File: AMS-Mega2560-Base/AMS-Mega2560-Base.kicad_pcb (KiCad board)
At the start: 4 copper layers, 168.7 x 106.7 mm, 224 parts, among them IC1 CD74HC4050ME4, IC10 LM2597MX-ADJ_NOPB, IC11 LM2597M-3.3_NOPB, IC12 OPA2340PA, IC13 MAX764CPA+, IC14 LM2917N-8_NOPB, IC15 MAX31865AAP+, IC16 DS3231SN#, IC17 MAX232CPE+, IC18 MAX31865AAP+, IC19 MAX6326UR31+T, IC2 CD74HC4050ME4, IC3 MAX31865AAP+, IC4 MAX31865AAP+, IC5 MAX31865AAP+, IC6 OPA2340PA, IC7 LTV-846S, IC8 MAX31865AAP+, IC9 LM2670SX-5.0_NOPB, J1 RTD1, J10 Conn_01x03, J11 Conn_01x02, J12 Conn_01x02, J13 Conn_01x03, J14 Conn_01x02, J15 Conn_01x02, J16 Conn_01x03, J17 Conn_01x02, J18 Conn_01x02, J19 Conn_01x03, J2 RTD2, J20 Conn_01x02, J21 Screw_Terminal_01x03, J22 Conn_01x07, J23 Conn_01x02, J24 Conn_01x02, J25 Conn_01x02, J26 Conn_01x03, J27 Conn_01x02, J28 Conn_01x02, J29 Conn_01x03, J3 Conn_01x08, J30 Conn_01x02, J31 Conn_01x02, J32 Conn_01x02, J4 Sense1, J5 Sense2, J6 AdafruitUltimateGPS, J7 Conn_02x03_Odd_Even, J8 Conn_01x03, J9 Conn_01x02, P1 Power, P10 CONN_01X01, P11 CONN_01X01, P12 CONN_01X01, P13 CONN_01X01, P2 Analog, P3 Analog, P4 Digital, P5 PWM, P6 PWM, P7 Communication, P8 CONN_01X01, P9 CONN_01X01, Q1 2N7000, Q10 IRF9Z34NPBF, Q11 2N7000, Q12 2N7000, Q13 IRF9Z34NPBF, Q14 IRF9Z34NPBF, Q15 2N7000, Q16 2N7000, Q17 IRF9Z34NPBF, Q18 IRF9Z34NPBF, Q19 2N7000, Q2 2N7000, Q20 IRF9Z34NPBF, Q21 IRF9Z34NPBF, Q22 BD140, Q23 2N7000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

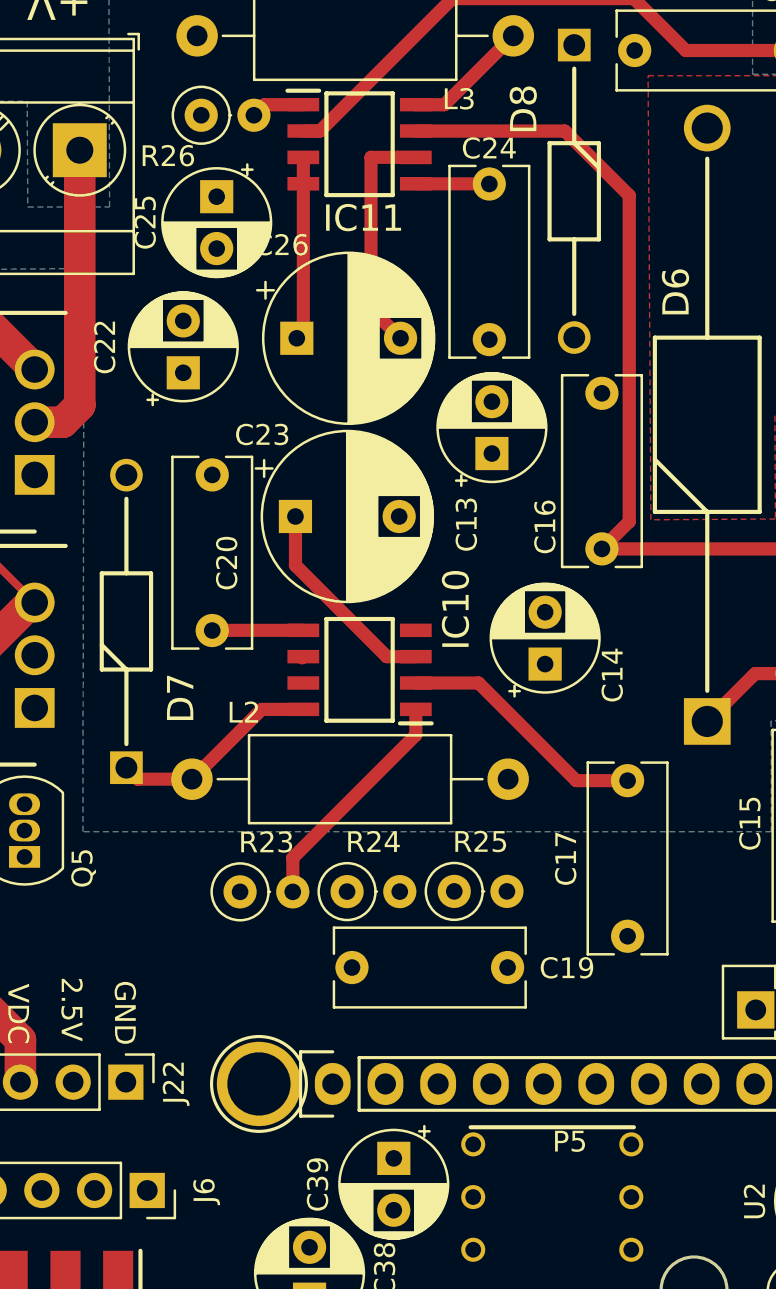
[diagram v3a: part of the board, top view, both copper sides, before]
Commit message: Schematic ERC is done and DRC for current layout is done. Need to verify a new part of the circuit before routing the rest of the board.
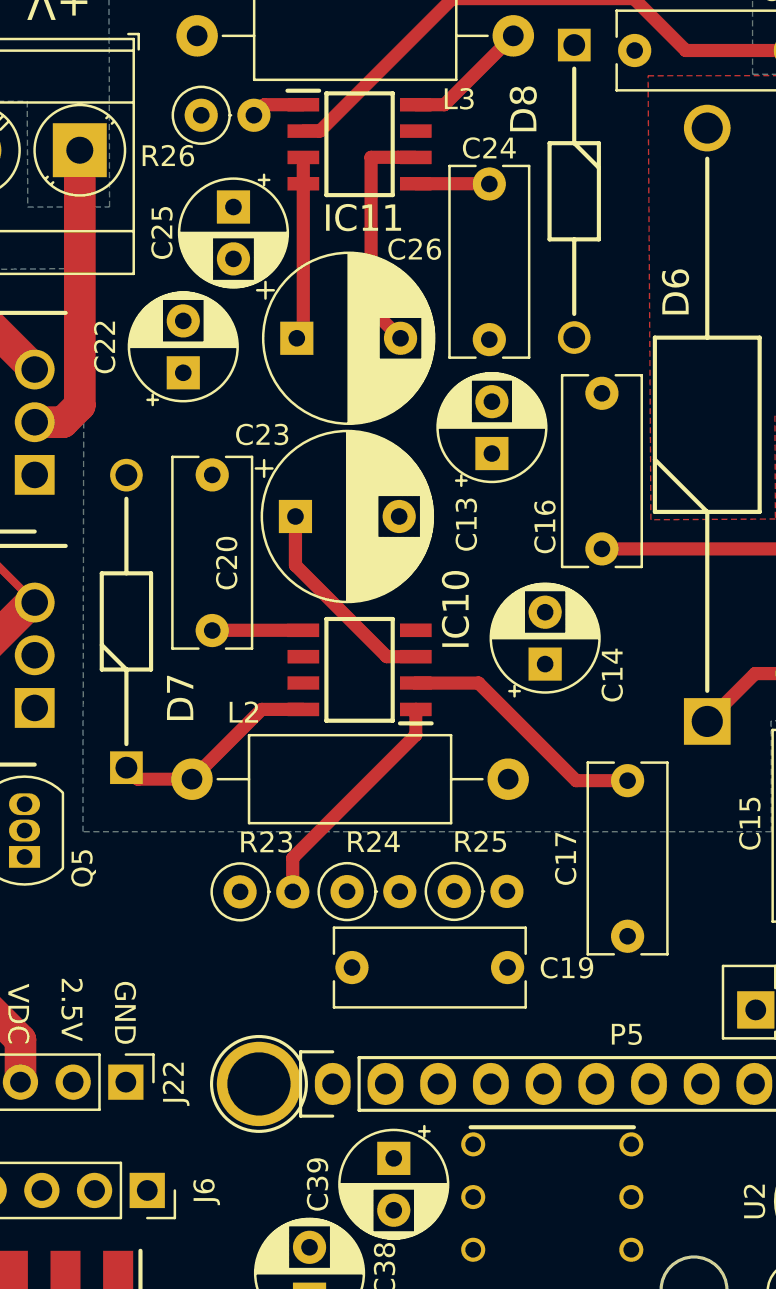
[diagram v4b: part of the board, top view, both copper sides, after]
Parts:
- moved C25 0.95 mm to (98.1, 58.5)
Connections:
- net /Ambient renamed 3VAmbientCS
- net /Carb renamed 3VCarbCS
- net /FrontT renamed 3VFrontCS
- net /LsideT renamed 3VLsideCS
- net /RsideT renamed 3VRsideCS
- net /WaterT renamed 3VWaterCS
- net IN1 renamed IN1TTL
- net IN2 renamed IN2TTL
- net IN3 renamed IN3TTL
- C18 pad 1: +5VP -> +5V
- C36 pad 1: +5VP -> +5V
- C40 pad 2: +5VP -> +5V
- IC1 pad 2: SCLK -> 3VSCLK
- IC1 pad 4: MOSI -> 3VMOSI
- IC1 pad 7: MISO -> 3VMISO
- IC12 pad 8: +5VP -> +5V
- IC15 pad 14: MOSI -> 3VMOSI
- IC15 pad 15: SCLK -> 3VSCLK
- IC15 pad 17: MISO -> 3VMISO
- IC16 pad 2: +5VP -> +5V
- IC17 pad 16: +5VP -> +5V
- IC18 pad 14: MOSI -> 3VMOSI
- IC18 pad 15: SCLK -> 3VSCLK
- IC18 pad 17: MISO -> 3VMISO
- IC3 pad 14: MOSI -> 3VMOSI
- IC3 pad 15: SCLK -> 3VSCLK
- IC3 pad 17: MISO -> 3VMISO
- IC4 pad 14: MOSI -> 3VMOSI
- IC4 pad 15: SCLK -> 3VSCLK
- IC4 pad 17: MISO -> 3VMISO
- IC5 pad 14: MOSI -> 3VMOSI
- IC5 pad 15: SCLK -> 3VSCLK
- IC5 pad 17: MISO -> 3VMISO
- IC8 pad 14: MOSI -> 3VMOSI
- IC8 pad 15: SCLK -> 3VSCLK
- IC8 pad 17: MISO -> 3VMISO
- IC9 pad 6: +5VP -> +5V
- J22 pad 4: +5VP -> +5V
- J3 pad 1: +5VP -> +5V
- J6 pad 1: /3.3 -> unconnected-(J6-Pad1)
- J6 pad 2: /EN -> unconnected-(J6-Pad2)
- J6 pad 4: /FIX -> unconnected-(J6-Pad4)
- J6 pad 8: +5VP -> +5V
- J6 pad 9: /PPS -> unconnected-(J6-Pad9)
- J7 pad 1: +5VP -> +5V
- L1 pad 2: +5VP -> +5V
- P1 pad 2: /IOREF -> unconnected-(P1-Pad2)
- P1 pad 3: /Reset -> unconnected-(P1-Pad3)
- P1 pad 4: +3V3 -> unconnected-(P1-Pad4)
- P1 pad 5: +5V -> unconnected-(P1-Pad5)
- P3 pad 7: /A14 -> unconnected-(P3-Pad7)
- P3 pad 8: /A15 -> unconnected-(P3-Pad8)
- P4 pad 16: /41 -> unconnected-(P4-Pad16)
- P4 pad 18: /39 -> unconnected-(P4-Pad18)
- P4 pad 20: /37 -> unconnected-(P4-Pad20)
- P4 pad 22: /35 -> unconnected-(P4-Pad22)
- P4 pad 23: /32 -> unconnected-(P4-Pad23)
- P4 pad 24: /33 -> unconnected-(P4-Pad24)
- P4 pad 25: /30 -> unconnected-(P4-Pad25)
- P4 pad 26: /31 -> unconnected-(P4-Pad26)
- P4 pad 27: /28 -> unconnected-(P4-Pad27)
- P4 pad 28: /29 -> unconnected-(P4-Pad28)
- P4 pad 29: /26 -> unconnected-(P4-Pad29)
- P4 pad 30: /27 -> unconnected-(P4-Pad30)
- P4 pad 31: /24 -> unconnected-(P4-Pad31)
- P4 pad 32: /25 -> unconnected-(P4-Pad32)
- P4 pad 33: /22 -> unconnected-(P4-Pad33)
- P4 pad 34: /23 -> unconnected-(P4-Pad34)
- P4 pad 35: +5V -> unconnected-(P4-Pad35)
- P4 pad 36: +5V -> unconnected-(P4-Pad36)
- P4 pad 4: /53(SS) -> unconnected-(P4-Pad4)
- P5 pad 3: /AREF -> unconnected-(P5-Pad3)
- P5 pad 5: /13(**) -> unconnected-(P5-Pad5)
- P5 pad 6: /12(**) -> unconnected-(P5-Pad6)
- P5 pad 7: /11(**) -> unconnected-(P5-Pad7)
- P5 pad 8: /10(**) -> unconnected-(P5-Pad8)
- P5 pad 9: /9(**) -> unconnected-(P5-Pad9)
- P6 pad 7: /1(Tx0) -> unconnected-(P6-Pad7)
- P6 pad 8: /0(Rx0) -> unconnected-(P6-Pad8)
- P7 pad 5: /18(Tx1) -> unconnected-(P7-Pad5)
- P7 pad 6: /19(Rx1) -> unconnected-(P7-Pad6)
- R1 pad 1: +5VP -> +5V
- R11 pad 1: +5VP -> +5V
- R13 pad 1: +5VP -> +5V
- R14 pad 1: +5VP -> +5V
- R15 pad 1: +5VP -> +5V
- R16 pad 1: +5VP -> +5V
- R17 pad 1: +5VP -> +5V
- R18 pad 1: +5VP -> +5V
- R19 pad 1: +5VP -> +5V
- R31 pad 1: +5VP -> +5V
- R37 pad 1: +5VP -> +5V
- R38 pad 1: +5VP -> +5V
- RV4 pad 1: AUXVoltage1 -> Sense1-11
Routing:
- net +VSW: track 92.2 -> 61.4 mm
- net +5VP: track 28.1 -> 0.00 mm
- net +5V: track 0.00 -> 28.1 mm

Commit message: pushing this change to the repo need to vet some schematics
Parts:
- removed R64: 4.7K, Resistor_THT:R_Axial_DIN0207_L6.3mm_D2.5mm_P2.54mm_Vertical
- Q22: value BD140 -> IRF9610PBF-BE3; footprint Package_TO_SOT_THT:TO-126-3_Vertical -> SamacSys_Parts:TO254P465X1024X2050-3P
- moved Q24 122.8 mm to (156.5, 115.6)
- moved D10 121.6 mm to (149.9, 122.0)
- moved Q22 52.7 mm to (70.6, 95.9), turned to -90 degrees
- moved J22 3.18 mm to (94.4, 97.9)
- moved U1 2.87 mm to (73.4, 73.0)
- moved Q23 2.69 mm to (70.3, 89.5)
- moved R63 2.69 mm to (76.0, 88.3)
- moved IC7 0.73 mm to (83.8, 115.1)
- moved J21 0.62 mm to (91.3, 55.7)
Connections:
- Q1 pad 2: Sense1-10 -> Sense2-1
- Q22 pad 1: +3.3VP -> Net-(Q22-Pad1)
- Q22 pad 3: Net-(Q22-Pad3) -> +3.3VP
- R5 pad 1: Sense1-10 -> Sense2-1
- R63 pad 1: Net-(Q22-Pad3) -> Net-(Q22-Pad1)
- RV3 pad 1: Sense2-1 -> Sense1-10
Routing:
- net +VDC: track 169.9 -> 139.6 mm
- net Net-(Q6-Pad3): track 18.2 -> 17.0 mm
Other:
- board text added: "ON"

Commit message: adding some fixes for the RPM sensor and trying to fit everything on the board. WIp for FW
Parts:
- removed J32: Conn_01x02, Connector_PinHeader_2.54mm:PinHeader_1x02_P2.54mm_Vertical
- removed RV3: 500k, Potentiometer_THT:Potentiometer_Bourns_3296W_Vertical
- added IC20: OPA4340UA, SamacSys_Parts:SOIC127P600X175-14N, F.Cu at (24.3, 123.3)
- added K1: DIP05-1A72-12L, SamacSys_Parts:DIP051A7212L, F.Cu at (205.3, 82.8)
- added Q25: 2N7000, Package_TO_SOT_THT:TO-92_Inline, F.Cu at (212.5, 83.8)
- added R64: 47K, Resistor_THT:R_Axial_DIN0207_L6.3mm_D2.5mm_P2.54mm_Vertical, F.Cu at (30.6, 120.2)
- added R65: 47K, Resistor_THT:R_Axial_DIN0207_L6.3mm_D2.5mm_P2.54mm_Vertical, F.Cu at (30.6, 124.2)
- added R66: 47K, Resistor_THT:R_Axial_DIN0207_L6.3mm_D2.5mm_P2.54mm_Vertical, F.Cu at (36.7, 120.2)
- added R67: 47K, Resistor_THT:R_Axial_DIN0207_L6.3mm_D2.5mm_P2.54mm_Vertical, F.Cu at (30.6, 128.3)
- added R68: 47K, Resistor_THT:R_Axial_DIN0207_L6.3mm_D2.5mm_P2.54mm_Vertical, F.Cu at (47.0, 120.2)
- added R69: 47K, Resistor_THT:R_Axial_DIN0207_L6.3mm_D2.5mm_P2.54mm_Vertical, F.Cu at (53.1, 120.2)
- added R70: R, Resistor_THT:R_Axial_DIN0207_L6.3mm_D2.5mm_P2.54mm_Vertical, F.Cu at (215.0, 89.7)
- IC6: value OPA2340PA -> OPA4340UA; footprint SamacSys_Parts:DIP794W53P254L959H508Q8N -> SamacSys_Parts:SOIC127P600X175-14N
- moved C29 98.5 mm to (297.2, 65.6)
- moved J23 96.0 mm to (271.7, 92.5)
- moved C27 92.8 mm to (273.5, 77.6)
- moved D9 89.7 mm to (287.3, 59.5)
- moved L4 89.7 mm to (273.2, 55.9)
- moved C30 89.7 mm to (266.8, 65.9)
- moved IC13 89.7 mm to (280.0, 66.4)
- moved J24 66.3 mm to (282.3, 91.1)
- moved C28 56.6 mm to (262.1, 80.3)
- moved J31 42.0 mm to (153.3, 133.6)
- moved R46 8.93 mm to (154.9, 95.2)
- moved RV4 5.09 mm to (115.8, 126.8)
- moved C32 4.95 mm to (213.4, 96.6)
- moved R1 4.13 mm to (218.1, 89.7), turned to 90 degrees
- moved R35 3.41 mm to (215.5, 84.5)
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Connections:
- IC14 pad 5: +VDC -> +VSW
- IC17 pad 13: Sense2-8 -> Sense1-8
- IC17 pad 14: Sense2-11 -> Sense1-11
- IC6 pad 1: ThrottlePositionADC -> OilPressure
- IC6 pad 2: ThrottlePositionADC -> OilPressure
- IC6 pad 3: Net-(IC6-Pad3) -> Sense1-10
- IC6 pad 4: GND -> +5V
- IC6 pad 5: Net-(IC6-Pad5) -> Sense1-7
- IC6 pad 6: SpareBufferedADC -> AFR1
- IC6 pad 7: SpareBufferedADC -> AFR1
- IC6 pad 8: +5V -> AFR2
- J31 pad 1: Net-(IC6-Pad3) -> Net-(RV2-Pad2)
- J31 pad 2: Net-(J31-Pad2) -> /A10
- J4 pad 12: AltCurrent -> Sense1-12
- J4 pad 2: OilPressure -> SCL
- J4 pad 5: FuelPressure1 -> SDA
- J4 pad 6: AFR1 -> Sense1-6
- J4 pad 8: FuelPressure2 -> Sense1-8
- J4 pad 9: AFR2 -> Sense1-9
- J5 pad 2: SCL -> Sense2-2
- J5 pad 5: SDA -> Sense2-5
- Q10 pad 2: Sense1-7 -> Sense2-11
- Q13 pad 2: Sense2-6 -> Sense2-9
- Q14 pad 2: Sense1-4 -> Sense2-8
- Q17 pad 2: Sense2-3 -> Sense2-12
- Q18 pad 2: Sense1-1 -> Sense2-5
- Q20 pad 2: Sense2-12 -> Sense2-3
- Q9 pad 2: Sense2-9 -> Sense2-6
- R32 pad 1: Sense1-3 -> Net-(R32-Pad1)
- R35 pad 2: +VDC -> +VSW
- R6 pad 2: ThrottlePositionADC -> OilPressure
- R7 pad 2: SpareBufferedADC -> AFR1
- RV2 pad 2: /A10 -> Net-(RV2-Pad2)
- RV4 pad 1: Sense1-11 -> Sense1-3
- RV4 pad 2: Net-(J32-Pad2) -> /BufferedADC/ADCIN4
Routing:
- net Sense1-7: track 48.1 -> 0.00 mm
- net Sense1-4: track 42.1 -> 0.00 mm
- net Sense1-1: track 34.9 -> 0.00 mm
- net Sense2-11: track 0.00 -> 28.7 mm
- net Sense2-12: track 18.9 -> 40.9 mm, vias 0 -> 1
- net Sense2-3: track 54.4 -> 33.8 mm, vias 1 -> 0
- net Sense2-5: track 0.00 -> 18.5 mm
- net Sense2-8: track 0.00 -> 14.7 mm
- net Sense2-9: track 26.9 -> 35.3 mm
- net Sense2-6: track 34.4 -> 35.3 mm

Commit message: applying some fixes for the RPM sensor and other parts of the schem
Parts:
- removed C10, C11, C33, C34, C41, C42, C5, C7, C8: 0.33uF, Capacitor_SMD:C_0805_2012Metric_Pad1.18x1.45mm_HandSolder
- removed C12, C35, C43, C6, C9: 100nF, Capacitor_THT:C_Disc_D7.5mm_W5.0mm_P10.00mm
- removed IC1, IC2: CD74HC4050ME4, SamacSys_Parts:SOIC127P600X175-16N
- removed IC15, IC18, IC3, IC4, IC5, IC8: MAX31865AAP+, SamacSys_Parts:SOP65P778X199-20N
- removed J1: RTD1, SamacSys_Parts:1727751
- removed J10, J13, J16, J19, J26, J29: Conn_01x03, Connector_PinHeader_2.54mm:PinHeader_1x03_P2.54mm_Vertical
- removed J11, J12, J14, J15, J17, J18, J20, J25, J27, J28, J30, J9: Conn_01x02, Connector_PinHeader_2.54mm:PinHeader_1x02_P2.54mm_Vertical
- removed J2: RTD2, SamacSys_Parts:1727751
- removed J8: Conn_01x03, Connector_PinSocket_2.54mm:PinSocket_1x03_P2.54mm_Vertical
- removed R2, R20, R3, R36, R4, R60: 430, Resistor_THT:R_Axial_DIN0207_L6.3mm_D2.5mm_P2.54mm_Vertical
- added T1: Conn_01x08, Connector_PinSocket_2.54mm:PinSocket_1x08_P2.54mm_Vertical, F.Cu at (206.3, 78.0)
- added T2: Conn_01x08, Connector_PinSocket_2.54mm:PinSocket_1x08_P2.54mm_Vertical, F.Cu at (185.1, 97.2)
- added T3: Conn_01x08, Connector_PinSocket_2.54mm:PinSocket_1x08_P2.54mm_Vertical, F.Cu at (185.2, 133.3)
- added T4: Conn_01x08, Connector_PinSocket_2.54mm:PinSocket_1x08_P2.54mm_Vertical, F.Cu at (204.3, 133.3)
- added T5: Conn_01x08, Connector_PinSocket_2.54mm:PinSocket_1x08_P2.54mm_Vertical, F.Cu at (204.2, 97.2)
- added T6: Conn_01x08, Connector_PinSocket_2.54mm:PinSocket_1x08_P2.54mm_Vertical, F.Cu at (155.7, 141.1)
- C1, C2, C4: value 0.33uF -> 22nF; footprint Capacitor_SMD:C_0805_2012Metric_Pad1.18x1.45mm_HandSolder -> Capacitor_THT:C_Disc_D4.7mm_W2.5mm_P5.00mm; moved to F.Cu
- C3: value 100nF -> 22nF; footprint Capacitor_THT:C_Disc_D7.5mm_W5.0mm_P10.00mm -> Capacitor_THT:C_Disc_D4.7mm_W2.5mm_P5.00mm
- R10, R5, R8, R9: value R -> 1M
- R11, R13, R14, R15: value R -> 330
- R16, R17, R18, R19: value R -> 22k
- moved C1 130.9 mm to (98.4, 139.6), turned to -90 degrees
- moved D9 113.1 mm to (189.3, 115.9), turned to 90 degrees
- moved C2 108.6 mm to (119.5, 132.5), turned to -90 degrees
- moved R67 106.8 mm to (137.3, 122.1)
- moved IC20 106.8 mm to (131.1, 120.8)
- moved C3 105.3 mm to (114.8, 132.4), turned to -90 degrees
- moved J24 101.1 mm to (181.2, 92.9)
- moved R66 100.5 mm to (137.3, 119.1)
- moved C4 100.3 mm to (109.7, 133.4), turned to 180 degrees
- moved C29 95.6 mm to (218.1, 119.3)
- moved J23 94.3 mm to (177.4, 93.8)
- moved IC13 92.9 mm to (195.9, 105.9)
- moved R68 90.4 mm to (137.2, 125.2)
- moved C30 90.0 mm to (198.0, 123.9)
- moved R65 89.5 mm to (120.1, 124.1)
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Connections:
- C1 pad 1: +3.3VA -> Sense2-10
- C2 pad 1: +3.3VA -> Sense2-7
- C3 pad 1: /Ambient Temp/RTDin- -> Sense2-4
- C3 pad 2: /Ambient Temp/RTDIn+ -> GND
- C4 pad 1: +3.3VA -> Sense2-1
- P4 pad 16: unconnected-(P4-Pad16) -> RPMEN
- Q23 pad 3: +3.3VP -> Net-(Q22-Pad1)
- Q25 pad 2: +5V -> RPMEN
- R70 pad 1: +5V -> RPMEN
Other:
- board text removed: "2"
- board text removed: "2-3"
- board text removed: "2-4"
- board text removed: "3"
- board text removed: "Ambient Temp"
- board text removed: "CARB Temp"
- board text removed: "Front Temp"
- board text removed: "Left Side Temp"
- board text removed: "Right Side Temp"
- board text removed: "WaterTemp"

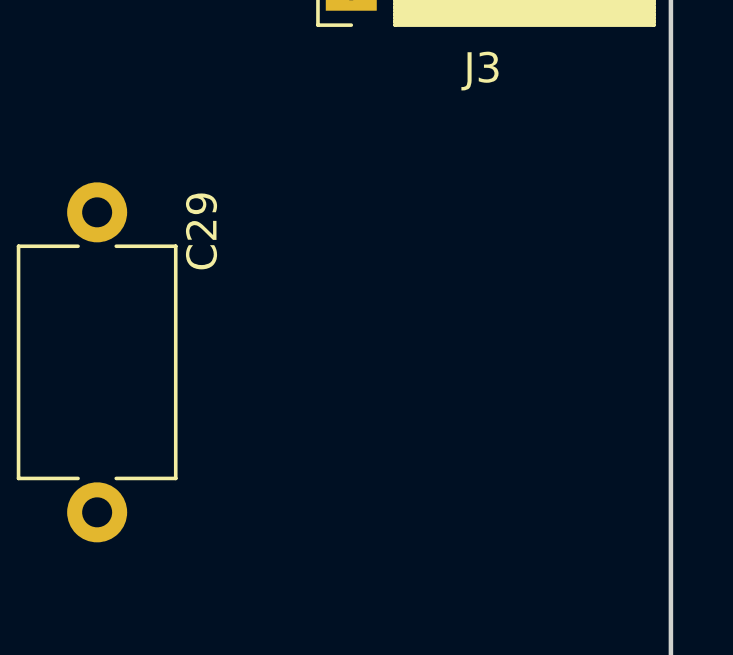
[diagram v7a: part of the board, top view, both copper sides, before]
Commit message: updated a few things for the SPI lines to the RTDs ready for routing.
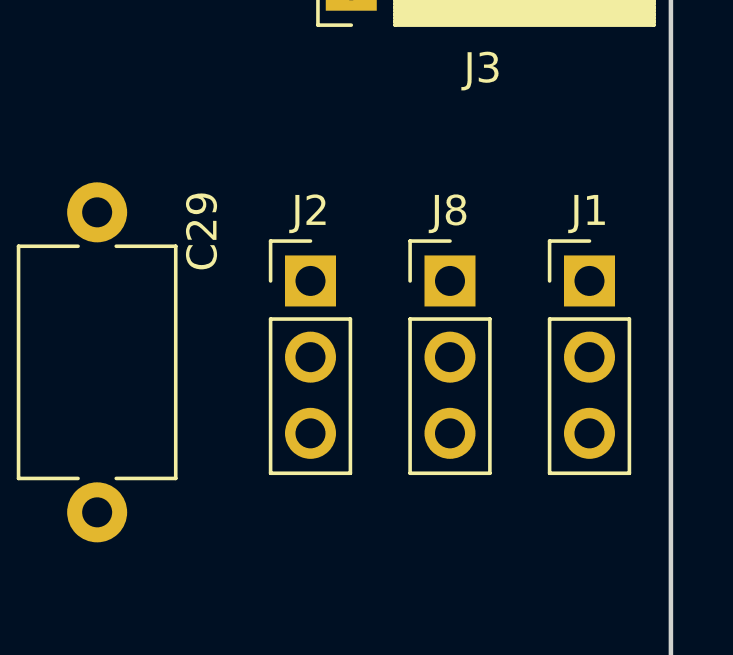
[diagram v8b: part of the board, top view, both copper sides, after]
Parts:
- added J1: Conn_01x03, Connector_PinHeader_2.54mm:PinHeader_1x03_P2.54mm_Vertical, F.Cu at (234.5, 121.5)
- added J2: Conn_01x03, Connector_PinHeader_2.54mm:PinHeader_1x03_P2.54mm_Vertical, F.Cu at (225.2, 121.5)
- added J8: Conn_01x03, Connector_PinHeader_2.54mm:PinHeader_1x03_P2.54mm_Vertical, F.Cu at (229.9, 121.5)
- C19: value C -> 3.3nF
- R70: value R -> 1M
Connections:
- T1 pad 4: SCLK -> RTDSCLK
- T1 pad 5: MISO -> RTDMISO
- T1 pad 6: MOSI -> RTDMOSI
- T2 pad 4: SCLK -> RTDSCLK
- T2 pad 5: MISO -> RTDMISO
- T2 pad 6: MOSI -> RTDMOSI
- T3 pad 4: SCLK -> RTDSCLK
- T3 pad 5: MISO -> RTDMISO
- T3 pad 6: MOSI -> RTDMOSI
- T4 pad 4: SCLK -> RTDSCLK
- T4 pad 5: MISO -> RTDMISO
- T4 pad 6: MOSI -> RTDMOSI
- T5 pad 4: SCLK -> RTDSCLK
- T5 pad 5: MISO -> RTDMISO
- T5 pad 6: MOSI -> RTDMOSI
- T6 pad 4: SCLK -> RTDSCLK
- T6 pad 5: MISO -> RTDMISO
- T6 pad 6: MOSI -> RTDMOSI
